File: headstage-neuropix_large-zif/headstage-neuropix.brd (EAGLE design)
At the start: 21.2 x 51.5 mm, 147 parts, among them J1 302-S101, J2 X.FL-R-SMT-1(02), J3 FH23-45S-0.3SHW(05), J4 77311-118-02LF, J5 FH23-45S-0.3SHW(05), U1 10M08SAM15317G, U10 BNO055, U11 DSC6102MI2A-093.6000, U12 PL133-27GC-R, U13 TS4231, U14 TS4231, U15 TS4231, U2 ASCO2-24.000MHZ-EK-T3, U3 MAX4945AELA+T, U4 ADP7112ACBZ-1.8-R7, U5 DS90UB933_WQFN, U6 NCP161BMX330, U7 TPS8268180, U8 TLV70712, U9 ADP7112ACBZ-1.2-R7, X2 OE-LOGO_14X10

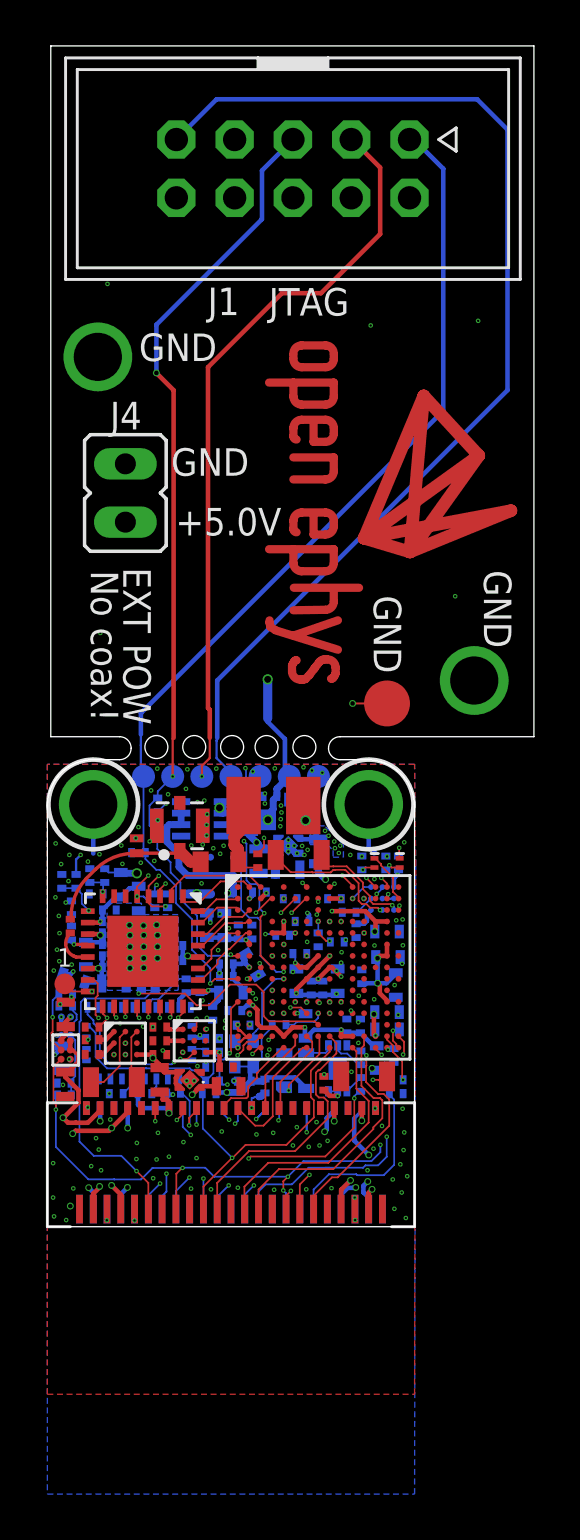
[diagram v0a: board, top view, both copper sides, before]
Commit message: Moved X.FL coax connector up 0.5 mm following OEPS feedback
- Allows more tolerance for passives under it
- Did this for both headstage variants
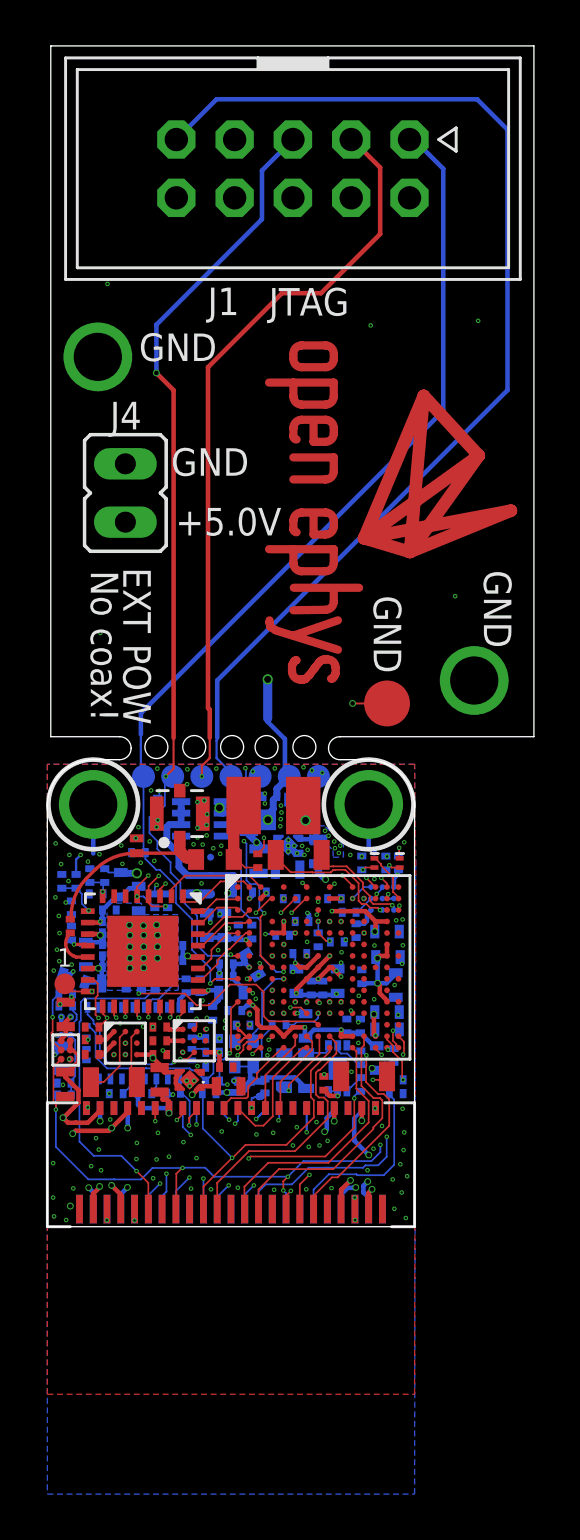
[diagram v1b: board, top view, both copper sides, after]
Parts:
- moved J2 0.53 mm to (-2.23, 17.0)
- moved L10 0.22 mm to (-0.70, 15.0)
- turned R8 to 270 degrees
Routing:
- net TMS: track 41.2 -> 42.0 mm
- net MIDFILT: track 4.76 -> 5.35 mm
- net GND: vias 193 -> 195
